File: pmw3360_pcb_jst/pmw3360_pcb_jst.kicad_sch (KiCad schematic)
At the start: 20 parts, among them J1 Conn_01x08, U1 PMW3360DM-T2QU, U2 TPS73601DBV

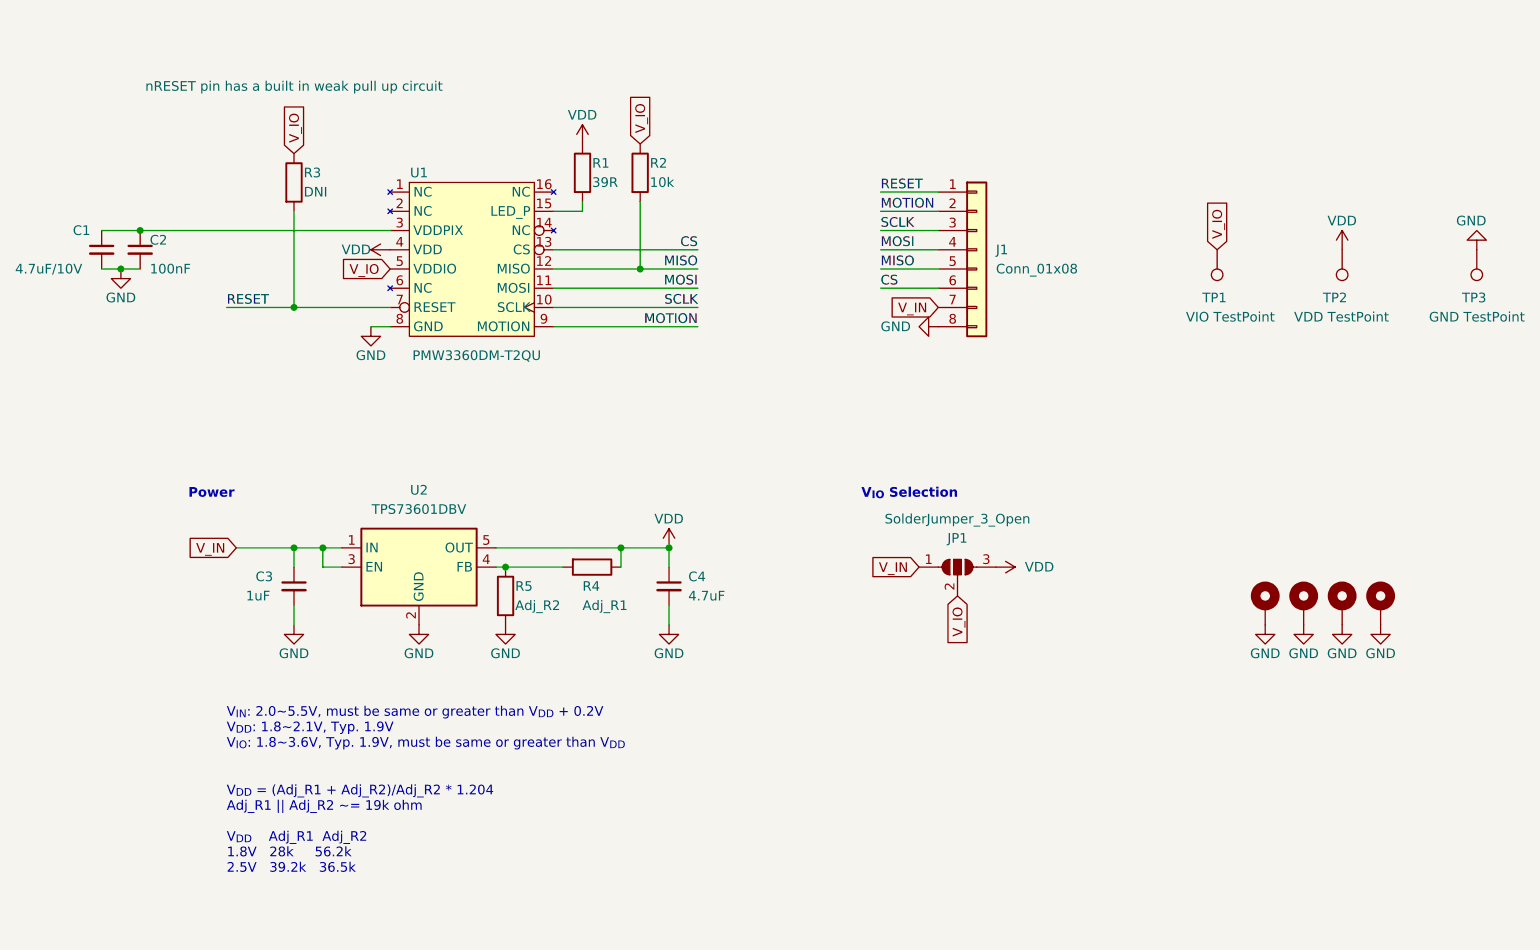
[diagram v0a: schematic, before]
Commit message: Update symbol references
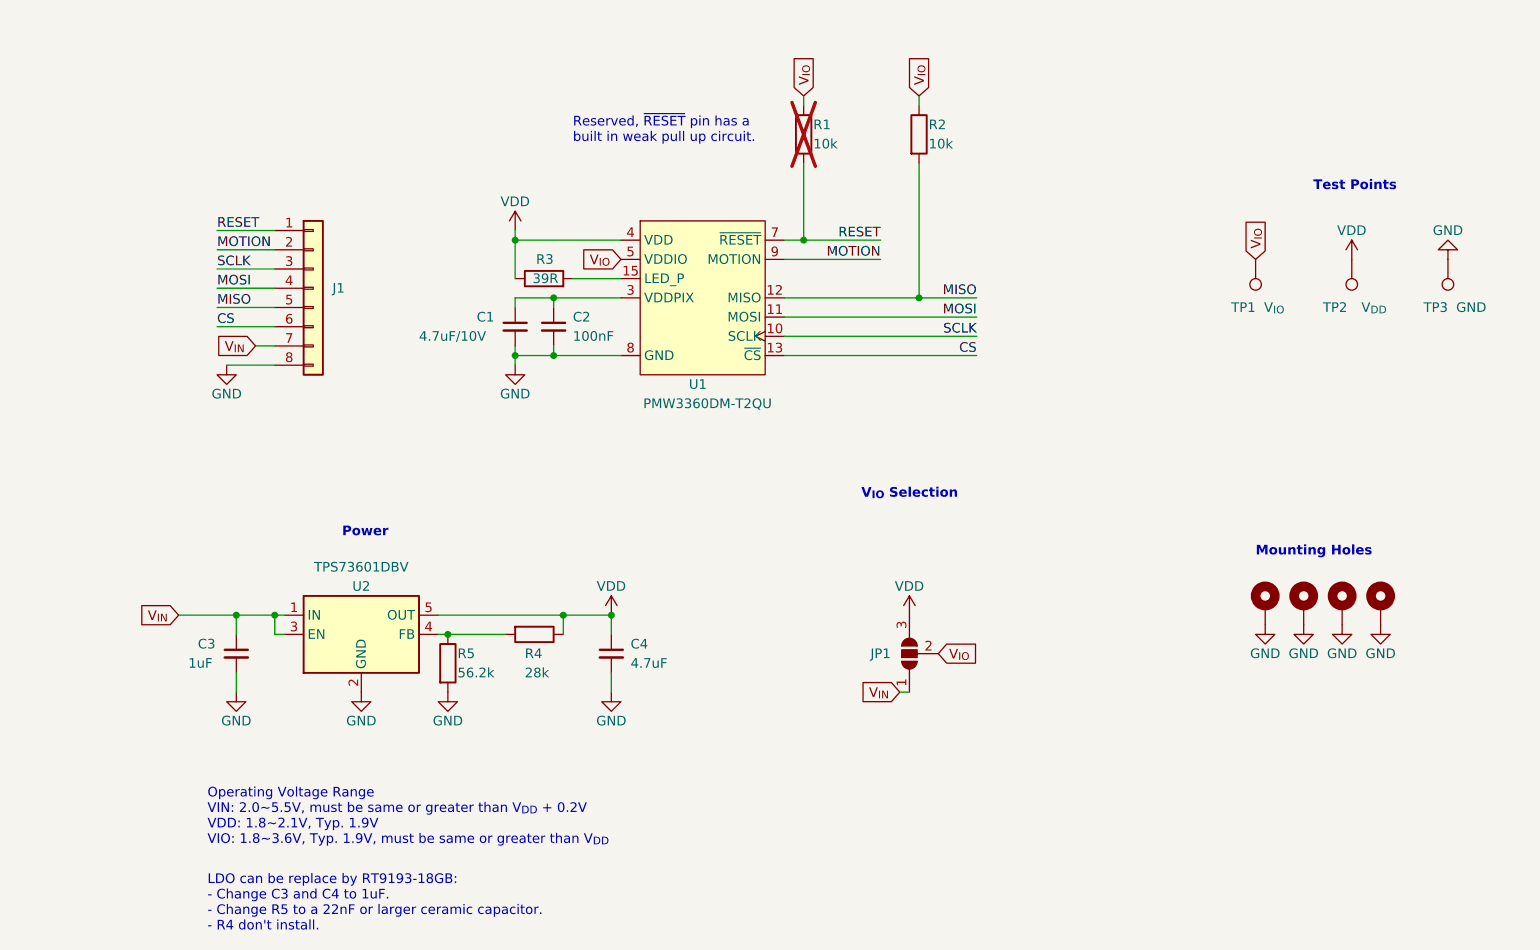
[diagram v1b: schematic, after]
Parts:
- JP1: footprint Jumper:SolderJumper-3_P1.3mm_Open_Pad1.0x1.5mm_NumberLabels -> Jumper:SolderJumper-3_P1.3mm_Open_RoundedPad1.0x1.5mm_NumberLabels
- R1: value 39R -> 10k; now not fitted
- R3: value DNI -> 39R; Note nRESET pin has a built in weak pull up circuit -> (none)
- R4: value Adj_R1 -> 28k
- R5: value Adj_R2 -> 56.2k
- TP1: value VIO TestPoint -> V_{IO}; footprint TestPoint:TestPoint_Pad_D1.5mm -> TestPoint:TestPoint_Pad_D1.0mm
- TP2: value VDD TestPoint -> V_{DD}; footprint TestPoint:TestPoint_Pad_D1.5mm -> TestPoint:TestPoint_Pad_D1.0mm
- TP3: value GND TestPoint -> GND; footprint TestPoint:TestPoint_Pad_D1.5mm -> TestPoint:TestPoint_Pad_D1.0mm
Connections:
- net RESET: now also R1.2; no longer R3.2
- net VDD: now also R3.1; no longer R1.1
- net at U1.15 (LED_P): now also R3.2; no longer R1.2
- net V_IN renamed V_{IN}
- net V_IO renamed V_{IO}
- net V_{IO}: now also R1.1; no longer R3.1
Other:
- note added: "LDO can be replace by RT9193-18GB: - Change C3 and C4 to 1uF. - Change R5 to a 22nF or larger ceramic capacitor. - R4 don't install."
- note added: "Mounting Holes"
- note added: "Operating Voltage Range VIN: 2.0~5.5V, must be same or greater than V_{DD} + 0.2V VDD: 1.8~2.1V, Typ. 1.9V VIO: 1.8~3.6V, Typ. 1.9V, must be same or greater than V_{DD}"
- note added: "Reserved, ~{RESET} pin has a built in weak pull up circuit."
- note added: "Test Points"
- note removed: "V_{DD} = (Adj_R1 + Adj_R2)/Adj_R2 * 1.204 Adj_R1 || Adj_R2 ~= 19k ohm V_{DD} Adj_R1 Adj_R2 1.8V 28k 56.2k 2.5V 39.2k 36.5k"
- note removed: "V_{IN}: 2.0~5.5V, must be same or greater than V_{DD} + 0.2V V_{DD}: 1.8~2.1V, Typ. 1.9V V_{IO}: 1.8~3.6V, Typ. 1.9V, must be same or greater than V_{DD}"
- moved on the sheet: J1
